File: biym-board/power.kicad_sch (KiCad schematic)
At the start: 9 parts, among them J1 HEADER_01X02_JST_SH_SMD_VERTI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, Q1 MOSFET-N-CH-EN, Q2 MOSFET-P-CH-EN, U1 BOOST_5V_RP402N501F

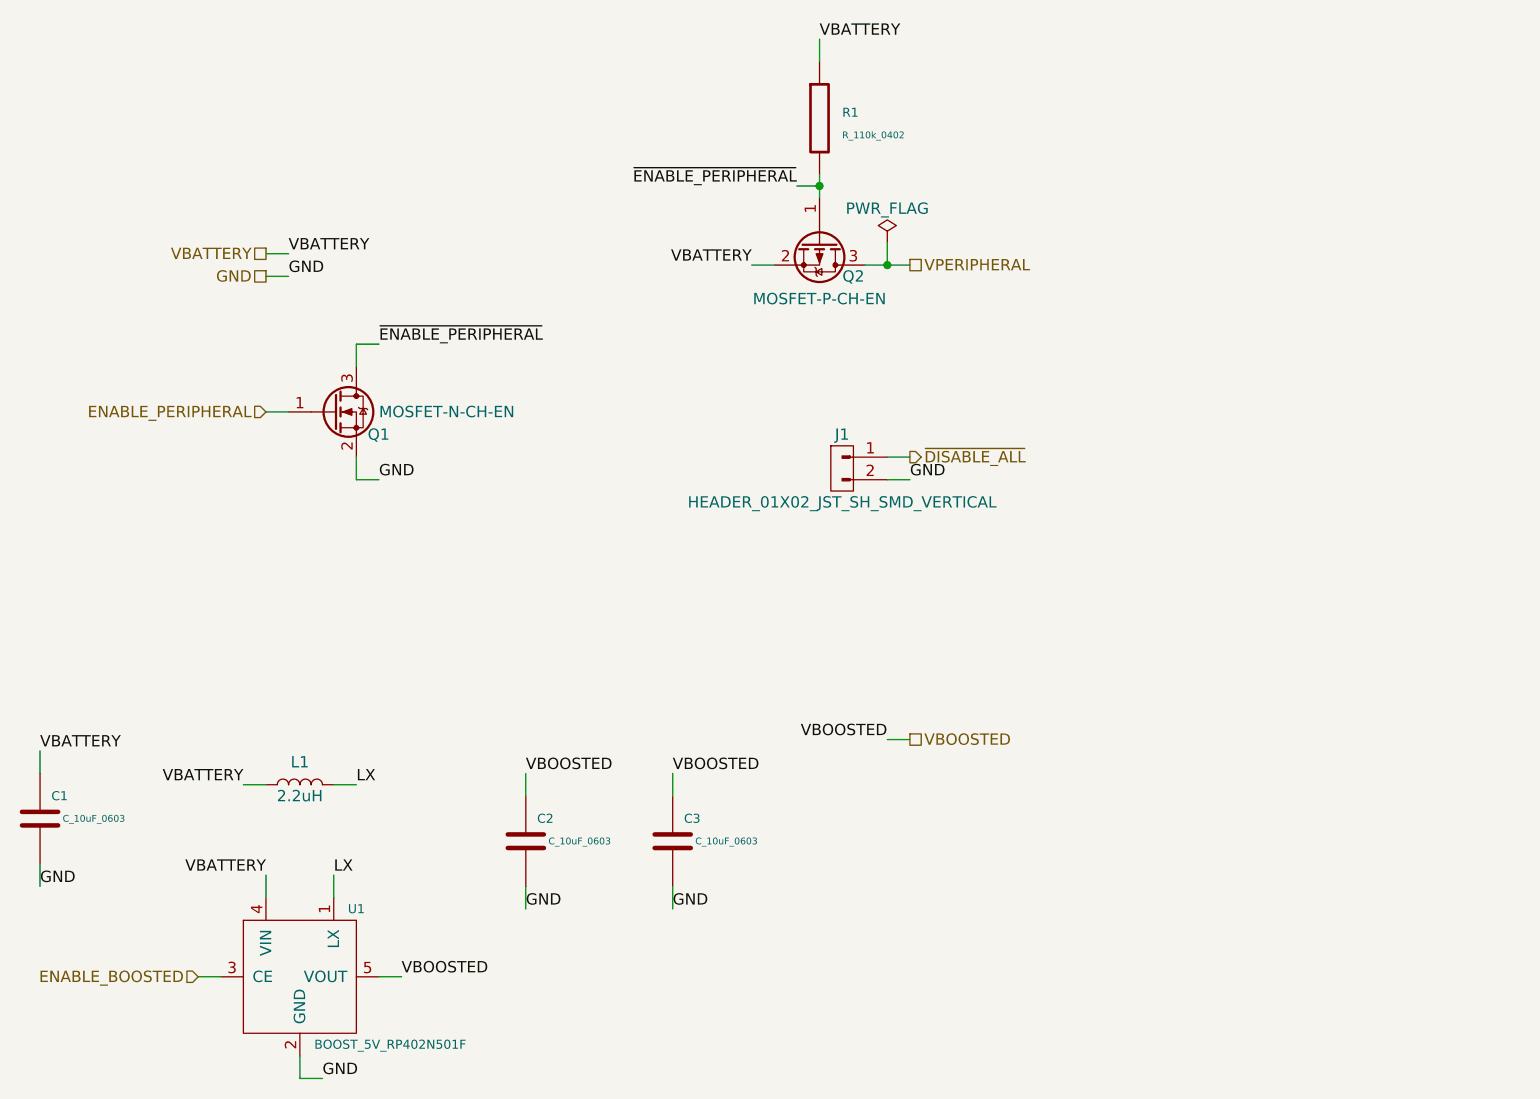
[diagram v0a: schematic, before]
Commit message: Add boost for both led and servo
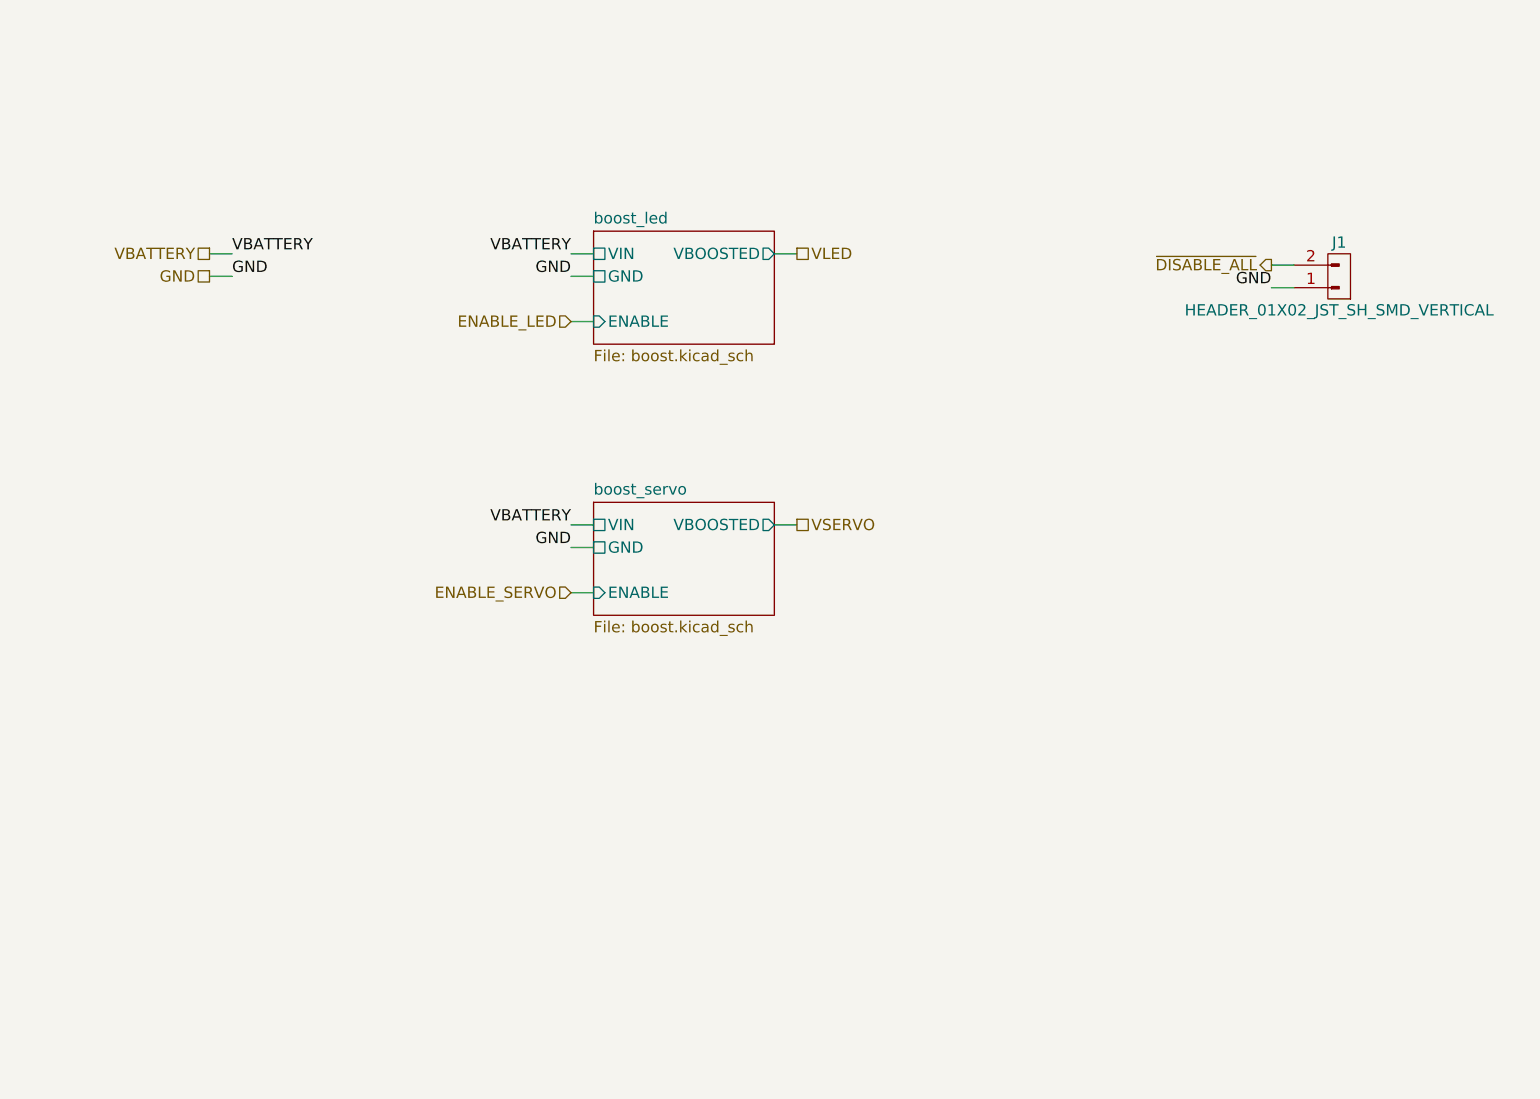
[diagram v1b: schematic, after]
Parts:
- removed C1, C2, C3: C_10uF_0603, Janelia:SM0603, symbol Janelia:C_10uF_0603
- removed L1: 2.2uH, Janelia:INDUCTOR_VLS_HBX, symbol Janelia:L_2.2uH_3A
- removed Q1: MOSFET-N-CH-EN, Janelia:SOT-23-3, symbol Janelia:MOSFET-N-CH-EN-DMG2302UKQ-7
- removed Q2: MOSFET-P-CH-EN, Janelia:SOT-23-3, symbol Janelia:MOSFET-P-CH-EN-DMP2045UQ-7
- removed R1: R_110k_0402, Janelia:SM0402, symbol Janelia:R_110k_0402
- removed U1: BOOST_5V_RP402N501F, Janelia:SOT-23-5, symbol Janelia:BOOST_5V_RP402N501F
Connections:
- net GND: now also J1.1 (Pin_1); no longer J1.2 (Pin_2)
- net ~{DISABLE_ALL}: now also J1.2 (Pin_2); no longer J1.1 (Pin_1)
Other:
- added sheet boost_led (boost.kicad_sch)
- added sheet boost_servo (boost.kicad_sch)
- moved on the sheet: J1

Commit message: Initial footprint placement
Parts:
- removed J1: HEADER_01X02_JST_SH_SMD_VERTICAL, Janelia:JST_SH_BM02B-SRSS-TB_1x02-1MP_P1.00mm_Vertical, symbol Janelia:HEADER_01X02_JST_SH_SMD_VERTICAL
- added J1: HEADER_01X02_JST_ZH_SMD_VERTICAL, Janelia:JST_ZH_B2B_ZR_SM4_TF_1x02-1MP_P1.50mm_Vertical, symbol Janelia:HEADER_01X02_JST_ZH_SMD_VERTICAL
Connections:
- net GND: now also J1.1 (Pin_1)
- net ~{DISABLE_ALL}: now also J1.2 (Pin_2)
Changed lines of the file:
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@@
     (effects (font (size 1.27 1.27)) (justify right))
   )
-  (symbol (lib_id "Janelia:HEADER_01X02_JST_SH_SMD_VERTICAL") (at 219.71 71.12 180) (unit 1)
+  (symbol (lib_id "Janelia:HEADER_01X02_JST_ZH_SMD_VERTICAL") (at 219.71 71.12 180) (unit 1)
     (in_bom yes) (on_board yes)
     (property "Reference" "J1" (id 0) (at 219.71 66.04 0))
-    (property "Value" "HEADER_01X02_JST_SH_SMD_VERTICAL" (id 1) (at 219.71 73.66 0))
-    (property "Footprint" "Janelia:JST_SH_BM02B-SRSS-TB_1x02-1MP_P1.00mm_Vertical" (id 2) (at 219.71 83.82 0)
+    (property "Value" "HEADER_01X02_JST_ZH_SMD_VERTICAL" (id 1) (at 219.71 73.66 0))
+    (property "Footprint" "Janelia:JST_ZH_B2B_ZR_SM4_TF_1x02-1MP_P1.50mm_Vertical" (id 2) (at 219.71 83.82 0)
       (effects (font (size 1.27 1.27)) hide)
     )
@@
       (effects (font (size 1.27 1.27)) hide)
     )
-    (property "Description" "CONN HEADER SMD 2POS 1MM" (id 4) (at 219.71 81.28 0)
+    (property "Description" "CONN HEADER SMD 2POS 1.5MM" (id 4) (at 219.71 81.28 0)
       (effects (font (size 1.27 1.27)) hide)
     )
@@
       (effects (font (size 1.27 1.27)) hide)
     )
-    (property "Manufacturer Part Number" "BM02B-SRSS-TB(LF)(SN)" (id 6) (at 219.71 86.36 0)
+    (property "Manufacturer Part Number" "B2B-ZR-SM4-TF(LF)(SN)" (id 6) (at 219.71 86.36 0)
       (effects (font (size 1.27 1.27)) hide)
     )
@@
       (effects (font (size 1.27 1.27)) hide)
     )
-    (property "Vendor Part Number" "455-1788-1-ND" (id 8) (at 219.71 93.98 0)
+    (property "Vendor Part Number" "B2B-ZR-SM4-TF(LF)(SN)" (id 8) (at 219.71 93.98 0)
       (effects (font (size 1.27 1.27)) hide)
     )

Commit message: Completed v1.1 layout
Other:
- sheet boost_led renamed boost-led
- sheet boost_servo renamed boost-servo
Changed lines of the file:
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@@
   (title_block
     (title "biym-board-power")
-    (date "2022-11-17")
-    (rev "1.0")
+    (date "2022-11-20")
+    (rev "1.1")
     (company "Peter Polidoro")
   )
@@
     (stroke (width 0.1524) (type solid) (color 0 0 0 0))
     (fill (color 0 0 0 0.0000))
-    (property "Sheet name" "boost_servo" (id 0) (at 135.89 94.5384 0)
+    (property "Sheet name" "boost-servo" (id 0) (at 135.89 94.5384 0)
       (effects (font (size 1.27 1.27)) (justify left bottom))
     )
@@
     (stroke (width 0.1524) (type solid) (color 0 0 0 0))
     (fill (color 0 0 0 0.0000))
-    (property "Sheet name" "boost_led" (id 0) (at 135.89 64.0584 0)
+    (property "Sheet name" "boost-led" (id 0) (at 135.89 64.0584 0)
       (effects (font (size 1.27 1.27)) (justify left bottom))
     )

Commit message: Update to kicad 7
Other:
- title: biym-board-power -> biym-board
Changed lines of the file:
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@@
-(kicad_sch (version 20211123) (generator eeschema)
+(kicad_sch (version 20230121) (generator eeschema)
   (paper "A4")
   (title_block
-    (title "biym-board-power")
-    (date "2022-11-29")
+    (title "biym-board")
+    (date "2024-05-16")
     (rev "1.3")
     (company "Peter Polidoro")
   )
   (wire (pts (xy 133.35 74.93) (xy 135.89 74.93))
-    (stroke (width 0) (type default) (color 0 0 0 0))
+    (stroke (width 0) (type default))
   )
   (wire (pts (xy 133.35 100.33) (xy 135.89 100.33))
-    (stroke (width 0) (type default) (color 0 0 0 0))
+    (stroke (width 0) (type default))
   )
   (wire (pts (xy 92.71 67.31) (xy 95.25 67.31))
-    (stroke (width 0) (type default) (color 0 0 0 0))
+    (stroke (width 0) (type default))
   )
   (wire (pts (xy 133.35 105.41) (xy 135.89 105.41))
-    (stroke (width 0) (type default) (color 0 0 0 0))
+    (stroke (width 0) (type default))
   )
   (wire (pts (xy 92.71 69.85) (xy 95.25 69.85))
-    (stroke (width 0) (type default) (color 0 0 0 0))
+    (stroke (width 0) (type default))
   )
   (wire (pts (xy 214.63 71.12) (xy 212.09 71.12))
-    (stroke (width 0) (type default) (color 0 0 0 0))
+    (stroke (width 0) (type default))
   )
   (wire (pts (xy 214.63 68.58) (xy 212.09 68.58))
-    (stroke (width 0) (type default) (color 0 0 0 0))
+    (stroke (width 0) (type default))
   )
   (wire (pts (xy 156.21 97.79) (xy 158.75 97.79))
-    (stroke (width 0) (type default) (color 0 0 0 0))
+    (stroke (width 0) (type default))
   )
   (wire (pts (xy 133.35 69.85) (xy 135.89 69.85))
-    (stroke (width 0) (type default) (color 0 0 0 0))
+    (stroke (width 0) (type default))
   )
   (wire (pts (xy 133.35 67.31) (xy 135.89 67.31))
-    (stroke (width 0) (type default) (color 0 0 0 0))
+    (stroke (width 0) (type default))
   )
   (wire (pts (xy 133.35 97.79) (xy 135.89 97.79))
-    (stroke (width 0) (type default) (color 0 0 0 0))
+    (stroke (width 0) (type default))
   )
   (wire (pts (xy 156.21 67.31) (xy 158.75 67.31))
-    (stroke (width 0) (type default) (color 0 0 0 0))
+    (stroke (width 0) (type default))
   )
-  (label "VBATTERY" (at 133.35 97.79 180)
+  (label "VBATTERY" (at 133.35 97.79 180) (fields_autoplaced)
     (effects (font (size 1.27 1.27)) (justify right bottom))
   )
-  (label "GND" (at 133.35 69.85 180)
+  (label "GND" (at 133.35 69.85 180) (fields_autoplaced)
     (effects (font (size 1.27 1.27)) (justify right bottom))
   )
-  (label "GND" (at 212.09 71.12 180)
+  (label "GND" (at 212.09 71.12 180) (fields_autoplaced)
     (effects (font (size 1.27 1.27)) (justify right bottom))
   )
-  (label "VBATTERY" (at 95.25 67.31 0)
+  (label "VBATTERY" (at 95.25 67.31 0) (fields_autoplaced)
     (effects (font (size 1.27 1.27)) (justify left bottom))
   )
-  (label "GND" (at 95.25 69.85 0)
+  (label "GND" (at 95.25 69.85 0) (fields_autoplaced)
     (effects (font (size 1.27 1.27)) (justify left bottom))
   )
-  (label "GND" (at 133.35 100.33 180)
+  (label "GND" (at 133.35 100.33 180) (fields_autoplaced)
     (effects (font (size 1.27 1.27)) (justify right bottom))
   )
-  (label "VBATTERY" (at 133.35 67.31 180)
+  (label "VBATTERY" (at 133.35 67.31 180) (fields_autoplaced)
     (effects (font (size 1.27 1.27)) (justify right bottom))
   )
-  (hierarchical_label "ENABLE_SERVO" (shape input) (at 133.35 105.41 180)
+  (hierarchical_label "ENABLE_SERVO" (shape input) (at 133.35 105.41 180) (fields_autoplaced)
     (effects (font (size 1.27 1.27)) (justify right))
   )
-  (hierarchical_label "GND" (shape passive) (at 92.71 69.85 180)
+  (hierarchical_label "GND" (shape passive) (at 92.71 69.85 180) (fields_autoplaced)
     (effects (font (size 1.27 1.27)) (justify right))
   )
-  (hierarchical_label "VBATTERY" (shape passive) (at 92.71 67.31 180)
+  (hierarchical_label "VBATTERY" (shape passive) (at 92.71 67.31 180) (fields_autoplaced)
     (effects (font (size 1.27 1.27)) (justify right))
   )
-  (hierarchical_label "VLED" (shape passive) (at 158.75 67.31 0)
+  (hierarchical_label "VLED" (shape passive) (at 158.75 67.31 0) (fields_autoplaced)
     (effects (font (size 1.27 1.27)) (justify left))
   )
-  (hierarchical_label "ENABLE_LED" (shape input) (at 133.35 74.93 180)
+  (hierarchical_label "ENABLE_LED" (shape input) (at 133.35 74.93 180) (fields_autoplaced)
     (effects (font (size 1.27 1.27)) (justify right))
   )
-  (hierarchical_label "VSERVO" (shape passive) (at 158.75 97.79 0)
+  (hierarchical_label "VSERVO" (shape passive) (at 158.75 97.79 0) (fields_autoplaced)
     (effects (font (size 1.27 1.27)) (justify left))
   )
-  (hierarchical_label "~{DISABLE_ALL}" (shape output) (at 212.09 68.58 180)
+  (hierarchical_label "~{DISABLE_ALL}" (shape output) (at 212.09 68.58 180) (fields_autoplaced)
     (effects (font (size 1.27 1.27)) (justify right))
   )
   (symbol (lib_id "Janelia:HEADER_01X02_JST_ZH_SMD_VERTICAL") (at 219.71 71.12 180) (unit 1)
-    (in_bom yes) (on_board yes)
-    (property "Reference" "J1" (id 0) (at 219.71 66.04 0))
-    (property "Value" "HEADER_01X02_JST_ZH_SMD_VERTICAL" (id 1) (at 219.71 73.66 0))
-    (property "Footprint" "Janelia:JST_ZH_B2B_ZR_SM4_TF_1x02-1MP_P1.50mm_Vertical" (id 2) (at 219.71 83.82 0)
+    (in_bom yes) (on_board yes) (dnp no)
+    (property "Reference" "J1" (at 219.71 66.04 0)
+      (effects (font (size 1.27 1.27)))
+    )
+    (property "Value" "HEADER_01X02_JST_ZH_SMD_VERTICAL" (at 219.71 73.66 0)
+      (effects (font (size 1.27 1.27)))
+    )
+    (property "Footprint" "Janelia:JST_ZH_B2B_ZR_SM4_TF_1x02-1MP_P1.50mm_Vertical" (at 219.71 83.82 0)
       (effects (font (size 1.27 1.27)) hide)
     )
-    (property "Datasheet" "" (id 3) (at 219.71 71.12 0)
+    (property "Datasheet" "" (at 219.71 71.12 0)
       (effects (font (size 1.27 1.27)) hide)
     )
-    (property "Description" "CONN HEADER SMD 2POS 1.5MM" (id 4) (at 219.71 81.28 0)
+    (property "Description" "CONN HEADER SMD 2POS 1.5MM" (at 219.71 81.28 0)
       (effects (font (size 1.27 1.27)) hide)
     )
-    (property "Manufacturer" "JST Sales America Inc." (id 5) (at 219.71 88.9 0)
+    (property "Manufacturer" "JST Sales America Inc." (at 219.71 88.9 0)
       (effects (font (size 1.27 1.27)) hide)
     )
-    (property "Manufacturer Part Number" "B2B-ZR-SM4-TF(LF)(SN)" (id 6) (at 219.71 86.36 0)
+    (property "Manufacturer Part Number" "B2B-ZR-SM4-TF(LF)(SN)" (at 219.71 86.36 0)
       (effects (font (size 1.27 1.27)) hide)
     )
-    (property "Vendor" "Digi-Key" (id 7) (at 219.71 91.44 0)
+    (property "Vendor" "Digi-Key" (at 219.71 91.44 0)
       (effects (font (size 1.27 1.27)) hide)
     )
-    (property "Vendor Part Number" "B2B-ZR-SM4-TF(LF)(SN)" (id 8) (at 219.71 93.98 0)
+    (property "Vendor Part Number" "B2B-ZR-SM4-TF(LF)(SN)" (at 219.71 93.98 0)
       (effects (font (size 1.27 1.27)) hide)
     )
     (pin "1")
     (pin "2")
+    (instances
+      (project "biym-board"
+        (path "/8aa5116f-ac54-4325-a42a-36123c2901d1/2c398cb1-cb17-49ba-86d6-22731656ead9"
+          (reference "J1") (unit 1)
+        )
+      )
+    )
   )
   (sheet (at 135.89 95.25) (size 20.32 12.7) (fields_autoplaced)
-    (stroke (width 0.1524) (type solid) (color 0 0 0 0))
+    (stroke (width 0.1524) (type solid))
     (fill (color 0 0 0 0.0000))
-    (property "Sheet name" "boost-servo" (id 0) (at 135.89 94.5384 0)
+    (property "Sheetname" "boost-servo" (at 135.89 94.5384 0)
       (effects (font (size 1.27 1.27)) (justify left bottom))
     )
-    (property "Sheet file" "boost.kicad_sch" (id 1) (at 135.89 108.5346 0)
+    (property "Sheetfile" "boost.kicad_sch" (at 135.89 108.5346 0)
       (effects (font (size 1.27 1.27)) (justify left top))
     )
@@
       (effects (font (size 1.27 1.27)) (justify left))
     )
+    (instances
+      (project "biym-board"
+        (path "/8aa5116f-ac54-4325-a42a-36123c2901d1/2c398cb1-cb17-49ba-86d6-22731656ead9" (page "9"))
+      )
+    )
   )
   (sheet (at 135.89 64.77) (size 20.32 12.7) (fields_autoplaced)
-    (stroke (width 0.1524) (type solid) (color 0 0 0 0))
+    (stroke (width 0.1524) (type solid))
     (fill (color 0 0 0 0.0000))
-    (property "Sheet name" "boost-led" (id 0) (at 135.89 64.0584 0)
+    (property "Sheetname" "boost-led" (at 135.89 64.0584 0)
       (effects (font (size 1.27 1.27)) (justify left bottom))
     )
-    (property "Sheet file" "boost.kicad_sch" (id 1) (at 135.89 78.0546 0)
+    (property "Sheetfile" "boost.kicad_sch" (at 135.89 78.0546 0)
       (effects (font (size 1.27 1.27)) (justify left top))
     )
@@
       (effects (font (size 1.27 1.27)) (justify left))
     )
+    (instances
+      (project "biym-board"
+        (path "/8aa5116f-ac54-4325-a42a-36123c2901d1/2c398cb1-cb17-49ba-86d6-22731656ead9" (page "8"))
+      )
+    )
   )
